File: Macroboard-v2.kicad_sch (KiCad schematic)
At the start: 0 parts

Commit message: 18:51 - 2025-5-21
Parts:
- added D1, D2: SK6812, LED_SMD:LED_SK6812_PLCC4_5.0x5.0mm_P3.2mm, symbol LED:SK6812
- added SW1, SW2, SW3, SW4: SW_Push, Button_Switch_Keyboard:SW_Cherry_MX_1.00u_PCB, symbol Switch:SW_Push
- added U1: XIAO-RP2040-DIP, OPKL:XIAO-RP2040-SMD, symbol OPKL:XIAO-RP2040-DIP
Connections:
- new net: SW3.2, U1.10 (GPIO4/MISO)
- new net: SW2.2, U1.9 (GPIO2/SCK)
- new net: SW4.2, U1.11 (GPIO3/MOSI)
- new net: D1.3 (VDD), U1.5 (GPIO6/SDA)
- new net: SW1.2, U1.8 (GPIO1/RX)
- new net: D1.1 (VSS), D2.3 (VDD)
- new net +5V: D1.4 (DOUT), D2.4 (DOUT), U1.14 (VBUS)
- new net GND: D1.2 (DIN), D2.2 (DIN), SW1.1, SW2.1, SW3.1, SW4.1, U1.13 (GND)

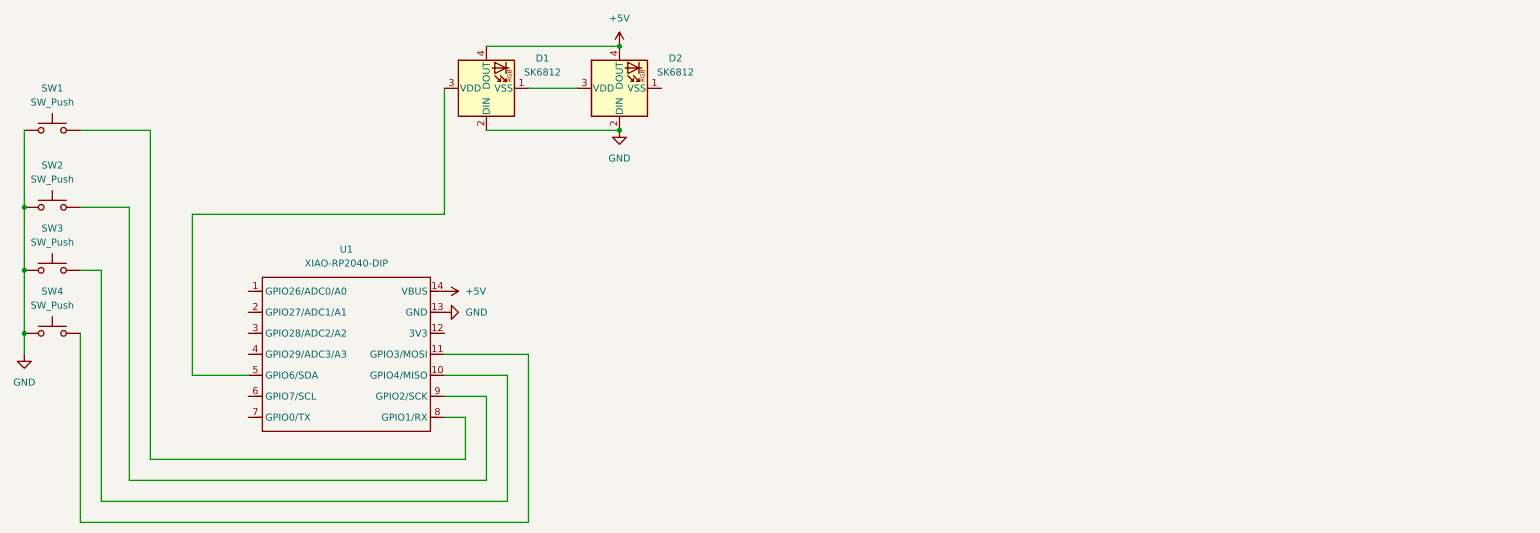
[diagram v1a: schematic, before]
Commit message: Adding Rotary Encoder to the macroboard . Added led Light and added Hot swapable switches
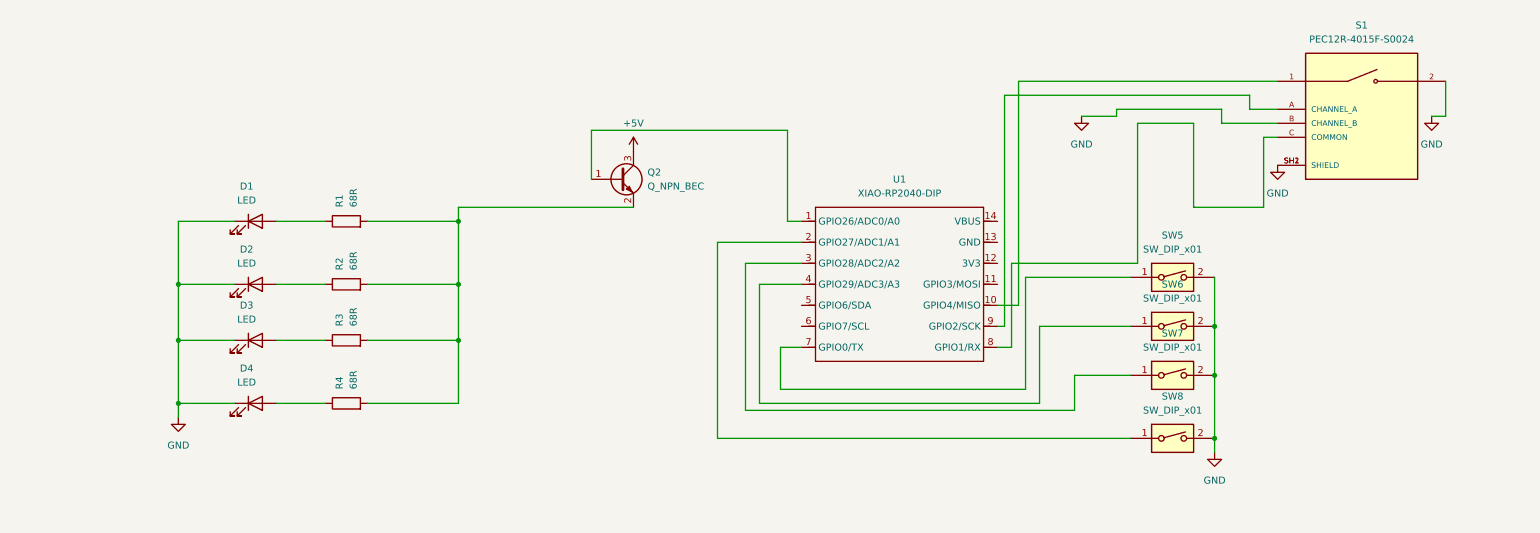
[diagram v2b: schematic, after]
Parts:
- removed D1, D2: SK6812, LED_SMD:LED_SK6812_PLCC4_5.0x5.0mm_P3.2mm, symbol LED:SK6812
- removed SW1, SW2, SW3, SW4: SW_Push, Button_Switch_Keyboard:SW_Cherry_MX_1.00u_PCB, symbol Switch:SW_Push
- added D1, D2, D3, D4: LED, LED_SMD:LED_1206_3216Metric, symbol Device:LED
- added Q2: Q_NPN_BEC, Package_TO_SOT_THT:TO-92, symbol Transistor_BJT:Q_NPN_BEC
- added R1, R2, R3, R4: 68R, Resistor_SMD:R_0603_1608Metric, symbol Device:R
- added S1: PEC12R-4015F-S0024, PEC12R-4015F-S0024:XDCR_PEC12R-4015F-S0024, symbol PEC12R-4015F-S0024 Rotary Encoder:PEC12R-4015F-S0024
- added SW5, SW6, SW7, SW8: SW_DIP_x01, MX Switch Hot Swapable:Kailh_socket_MX, symbol Switch:SW_DIP_x01
- U1: footprint OPKL:XIAO-RP2040-SMD -> OPKL:XIAO-RP2040-DIP
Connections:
- net +5V: now also Q2.3 (C); no longer U1.14 (VBUS)
- net GND: now also D1.1 (K), D2.1 (K), D3.1 (K), D4.1 (K), S1.2, S1.B (CHANNEL_B), S1.SH1 (SHIELD), S1.SH2 (SHIELD), SW5.2, SW6.2, SW7.2, SW8.2; no longer U1.13 (GND)
- net at U1.10 (GPIO4/MISO): now also S1.1
- net at U1.9 (GPIO2/SCK): now also S1.A (CHANNEL_A)
- net at U1.1 (GPIO26/ADC0/A0): now also Q2.1 (B)
- net at U1.2 (GPIO27/ADC1/A1): now also SW8.1
- net at U1.3 (GPIO28/ADC2/A2): now also SW7.1
- net at U1.4 (GPIO29/ADC3/A3): now also SW6.1
- net at U1.7 (GPIO0/TX): now also SW5.1
- net at U1.8 (GPIO1/RX): now also S1.C (COMMON)
- new net: D2.2 (A), R2.1
- new net: Q2.2 (E), R1.2, R2.2, R3.2, R4.2
- new net: D3.2 (A), R3.1
- new net: D1.2 (A), R1.1
- new net: D4.2 (A), R4.1

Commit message: Schemetics and PCB Desing completed . T- 1756 -20250522
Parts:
- removed S1: PEC12R-4015F-S0024, PEC12R-4015F-S0024:XDCR_PEC12R-4015F-S0024, symbol PEC12R-4015F-S0024 Rotary Encoder:PEC12R-4015F-S0024
- added S2: PEC12R-4015F-S0024, PEC12R-4015F-S0024 Rotary Encoder:XDCR_PEC12R-4015F-S0024, symbol PEC12R-4015F-S0024 Rotary Encoder:PEC12R-4015F-S0024
- Q2: footprint Package_TO_SOT_THT:TO-92 -> Transistor:SOT-23
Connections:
- net GND: now also S2.2, S2.B (CHANNEL_B), S2.SH1 (SHIELD), S2.SH2 (SHIELD)
- net at U1.10 (GPIO4/MISO): now also S2.1
- net at U1.8 (GPIO1/RX): now also S2.C (COMMON)
- net at U1.9 (GPIO2/SCK): now also S2.A (CHANNEL_A)
